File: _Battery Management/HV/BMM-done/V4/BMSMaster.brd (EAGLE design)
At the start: 83.8 x 91.4 mm, 113 parts, among them J1 M2S02B-PASK-2(LF)(SN), J10 IMD, J14 USB_B_RA, J2 M2S02B-PASK-2(LF)(SN), J3 M8S08B-PASK-2(LF)(SN), J5 M16_M_194280016, J6 M2770166, J7 M2770166, J8 M2770166, J9 M2770166, K1 ADJ14024, Q1 IRFR9120TRPBF, Q3 BSS123, U1 SN75HVD08DRMSOP, U10 NC7S14M5X, U11 LTC6820, U12 FT24C64A, U23 NUD3160DMT1G, U3 FT230X, U4 SN74LVC2G241, U5 NC7S14M5X, U6 DSPIC33FJ128GP804, U7 DMG6602SVTQ, U8 LTC6820, U9 MAX823TEUK+T_3.08, Y1 12Mhz

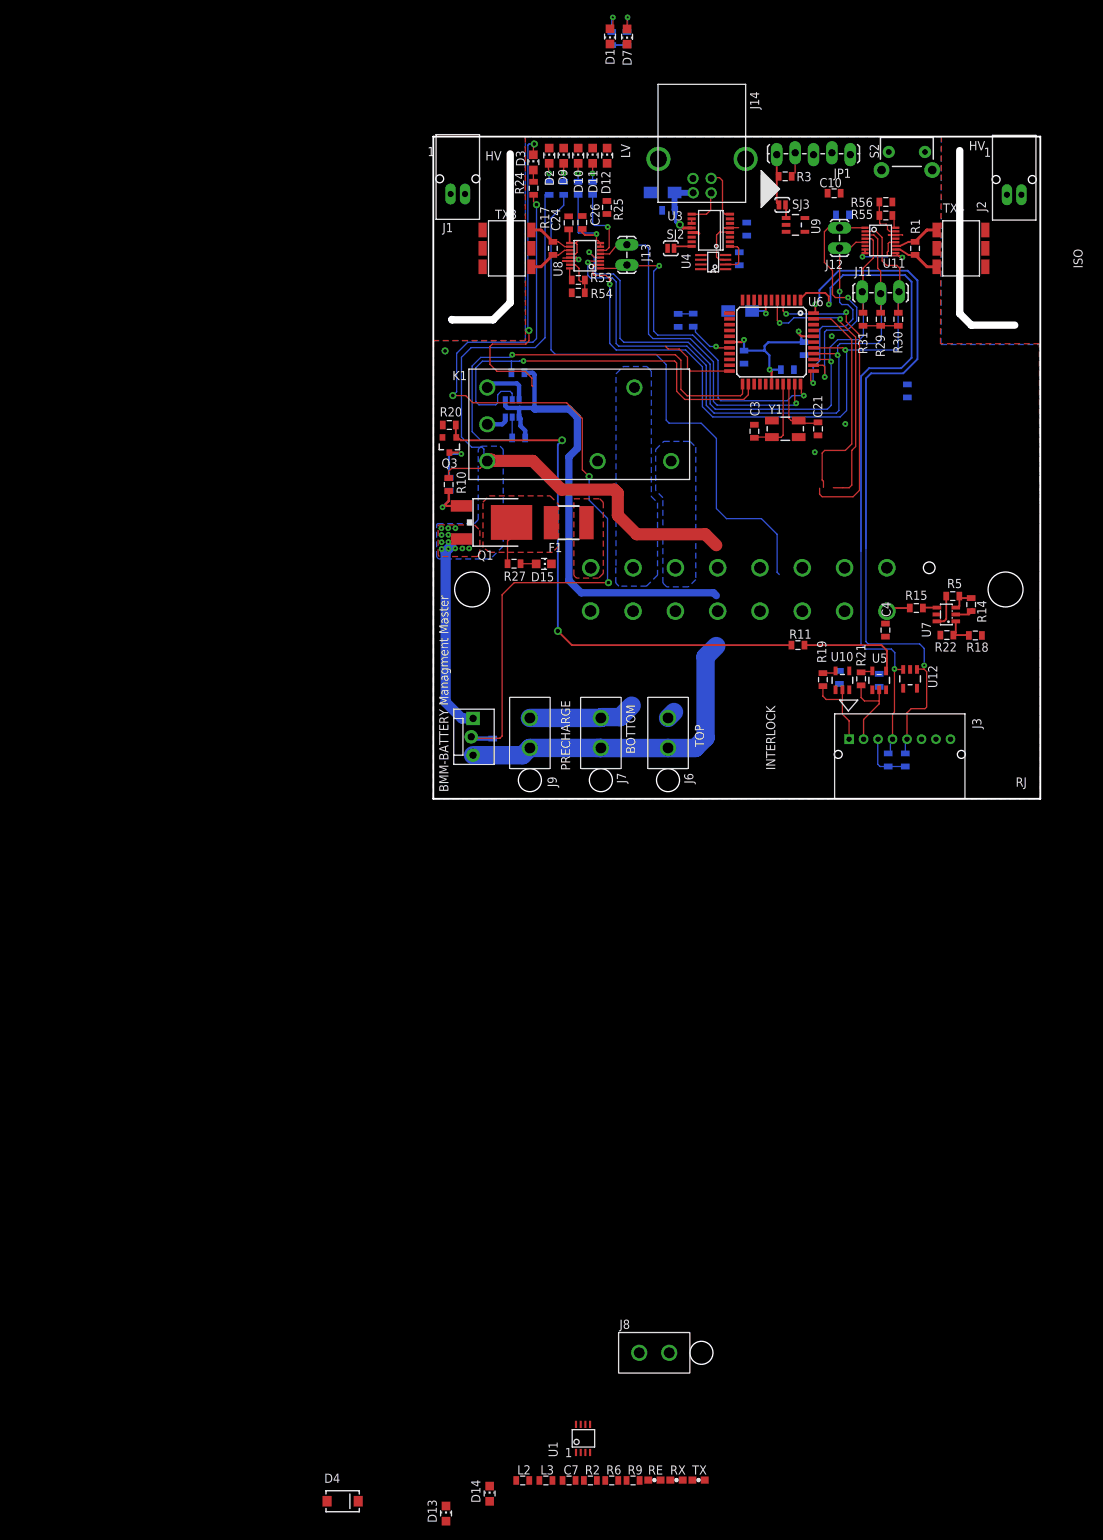
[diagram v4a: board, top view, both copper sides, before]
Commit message: Working on DC/DC power supply
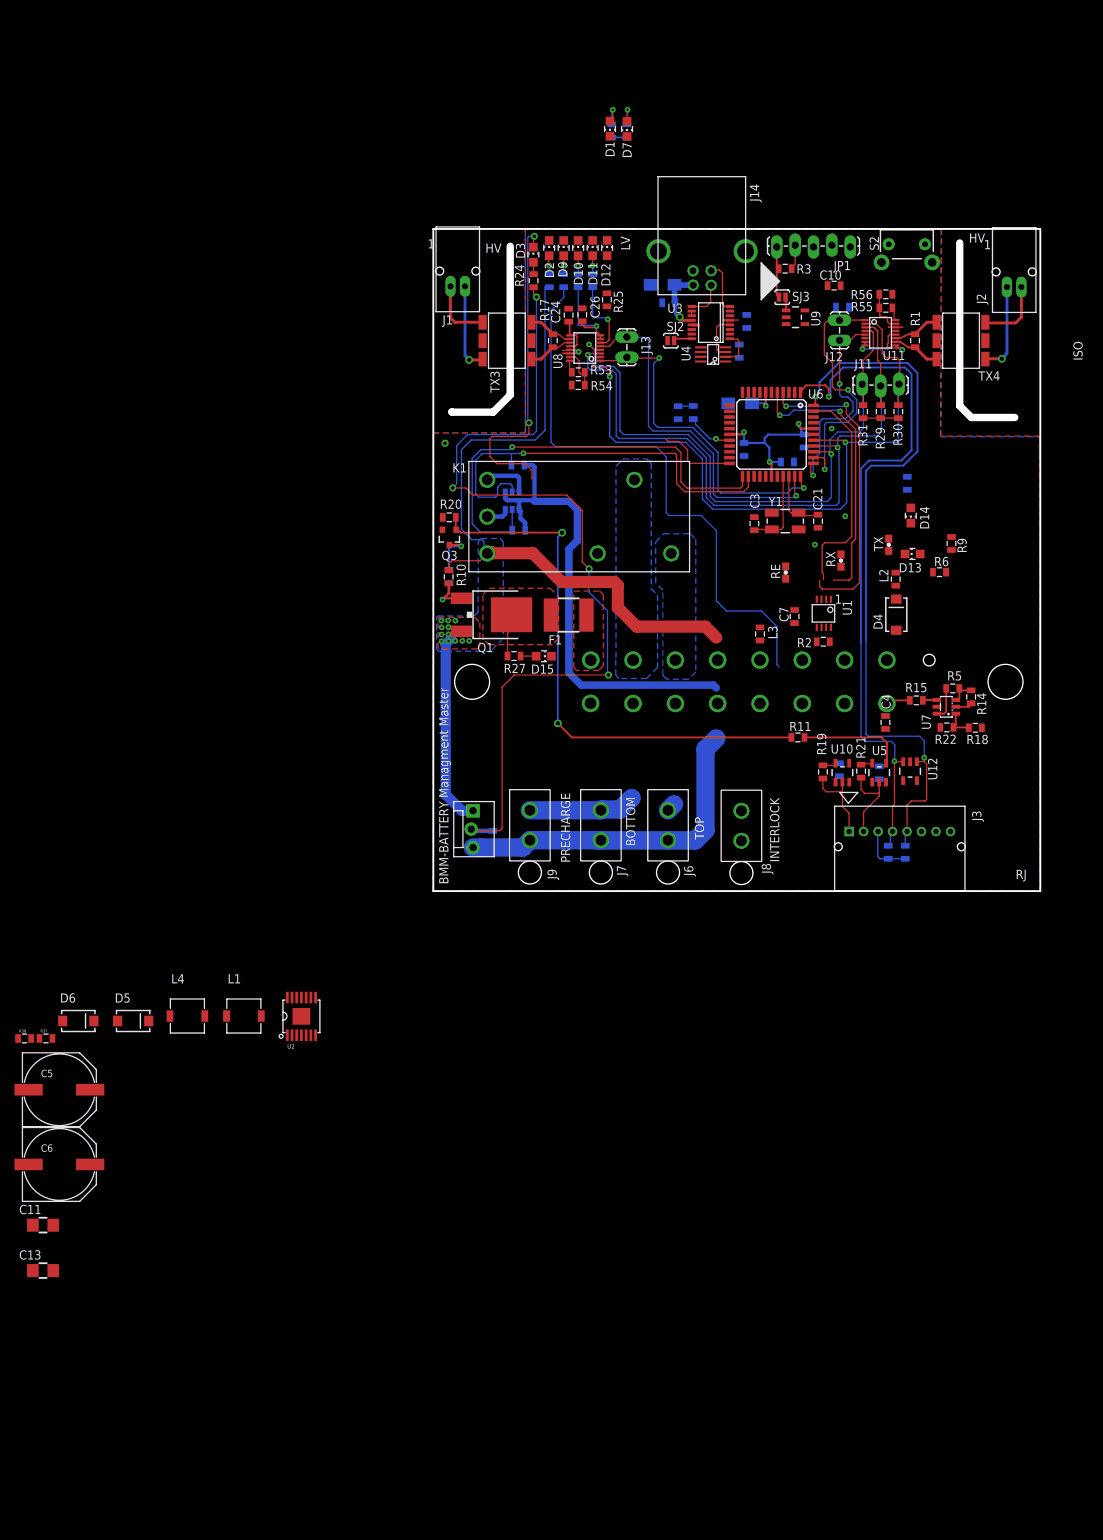
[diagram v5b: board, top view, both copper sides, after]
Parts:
- added C11, C13: 10UF, FSAE Electric:1206
- added C5, C6: 100UF, FSAE Electric:PANASONIC-G
- added D5, D6: DIODE_S1B, FSAE Electric:SMA
- added L1, L4: (no value), FSAE Electric:VLF5014AT
- added R37, R38: 20K, FSAE Electric:0805
- added U2: TPS54386PWPR, FSAE Electric:TSSOP-14
- moved D13 147.3 mm to (66.2, 46.5), turned to 90 degrees
- moved D14 147.1 mm to (65.9, 51.8), turned to 180 degrees
- moved D4 144.3 mm to (63.9, 38.1), turned to 90 degrees
- moved R9 136.7 mm to (71.6, 48.0), turned to 270 degrees
- moved L2 134.7 mm to (63.9, 43.0), turned to 270 degrees
- moved R6 133.3 mm to (69.9, 44.0)
- moved TX 131.8 mm to (62.9, 47.8), turned to 90 degrees
- moved RX 129.0 mm to (56.3, 45.6), turned to 90 degrees
- moved RE 126.6 mm to (48.7, 43.9), turned to 90 degrees
- moved C7 123.3 mm to (49.9, 37.9), turned to 90 degrees
- moved L3 120.6 mm to (45.1, 35.5), turned to 270 degrees
- moved R2 120.2 mm to (53.8, 34.4), turned to 180 degrees
- moved U1 118.7 mm to (53.9, 38.3), turned to 180 degrees
- moved J8 73.8 mm to (42.5, 8.97), turned to 270 degrees
- moved J2 12.8 mm to (80.2, 83.4)
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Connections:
- removed net N$60: L3.1
- new net N$56: L1.2, U2.3
- new net N$57: L4.1, U2.12
- new net N$59: R37.1, U2.7
- new net N$61: R38.1, U2.8
- net +3V3: now also C13.1, C6.+, L4.2, R38.2
- net +5V: now also C11.1, C5.+, L1.1, R37.2
- net +9V: now also U2.1, U2.14
- net GND: now also C11.2, C13.2, C5.-, C6.-, L3.1, U2.4, U2.5, U2.6, U2.EP
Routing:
- net N$55: track 0.00 -> 12.5 mm, vias 0 -> 1
- net N$33: track 0.00 -> 12.3 mm, vias 0 -> 1
- net N$53: track 0.00 -> 9.51 mm
- net N$34: track 0.00 -> 9.05 mm

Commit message: 
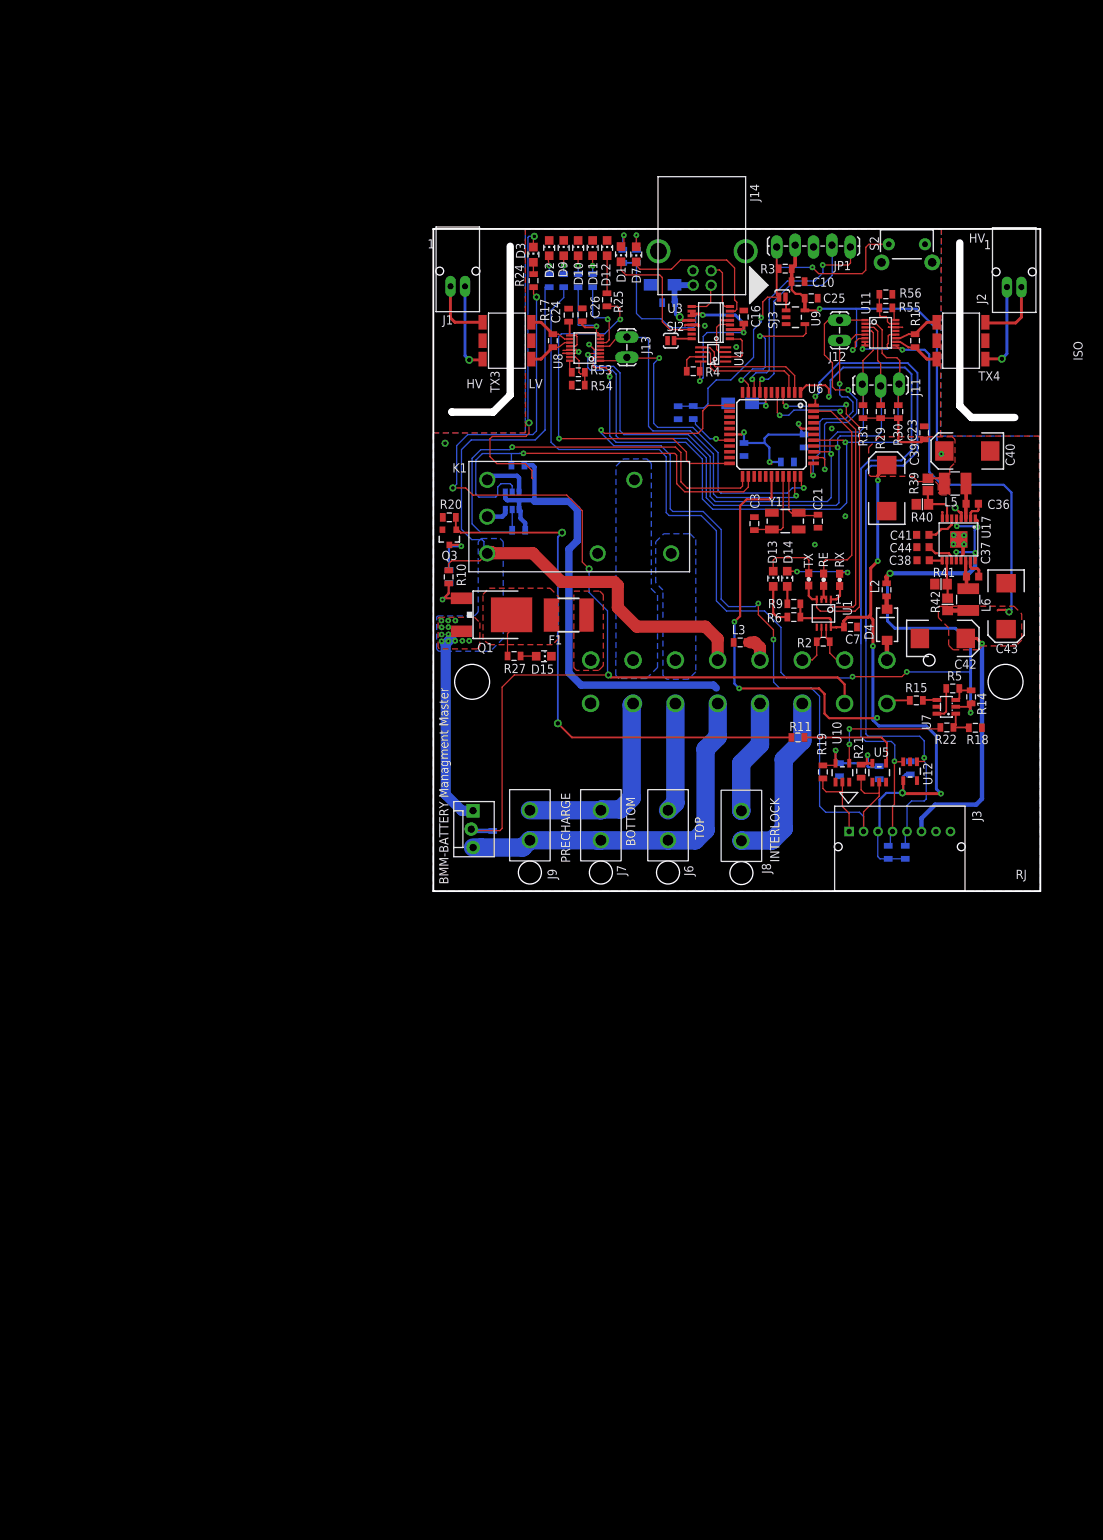
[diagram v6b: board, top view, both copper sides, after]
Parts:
- removed C11, C13: 10UF, FSAE Electric:1206
- removed C5, C6: 100UF, FSAE Electric:PANASONIC-G
- removed D5, D6: DIODE_S1B, FSAE Electric:SMA
- removed L1, L4: (no value), FSAE Electric:VLF5014AT
- removed R37, R38: 20K, FSAE Electric:0805
- removed U2: TPS54386PWPR, FSAE Electric:TSSOP-14
- added C36, C37: 0.1UF, DFT2:R0603
- added C38: 1UF, DFT2:R0603
- added C39, C40, C42, C43: 22UF, DFT2:EIA7343
- added C41, C44: 0.001UF, DFT2:R0603
- added L5: L_2.2UH, DFT2:LQH43
- added L6: L_4.7UH, DFT2:LQH43
- added R39: 73.2K, DFT2:R0805
- added R40, R41: 22.1K, DFT2:R0805
- added R42: 124K, DFT2:R0805
- added U17: TPS542951PWPR, DFT2:TSSOP-16
- moved R9 23.3 mm to (49.8, 39.6), turned to 0 degrees
- moved R6 21.0 mm to (49.8, 37.8)
- moved D13 19.6 mm to (46.9, 43.1), turned to 0 degrees
- moved D14 19.2 mm to (48.9, 43.1), turned to 0 degrees
- moved D1 17.4 mm to (25.9, 87.9)
- moved R7 17.4 mm to (26.2, 87.6)
- moved R8 17.4 mm to (28.1, 87.6)
- moved D7 17.4 mm to (28.0, 87.9)
- moved TX 12.0 mm to (51.8, 43.0)
- moved C7 7.86 mm to (57.6, 36.4), turned to 0 degrees
- moved C23 7.34 mm to (67.8, 63.2), flipped to the top, turned to 90 degrees
- moved C4 7.15 mm to (65.9, 17.0), flipped to the bottom, turned to 90 degrees
- moved R4 6.94 mm to (35.9, 71.7), flipped to the top, turned to 0 degrees
- moved RE 5.33 mm to (53.9, 43.0)
- moved C10 5.01 mm to (50.4, 84.1)
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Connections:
- removed net N$56: L1.2, U2.3
- removed net N$57: L4.1, U2.12
- removed net N$59: R37.1, U2.7
- removed net N$61: R38.1, U2.8
- new net N$100: C38.1, U17.9
- new net N$101: R39.1, R40.2, U17.7
- new net N$102: C41.1, U17.6
- new net N$103: R41.2, R42.1, U17.10
- new net N$77: C44.1, U17.11
- new net N$94: C36.1, U17.2
- new net N$97: C36.2, L5.2, U17.3
- new net N$98: C37.1, U17.15
- new net N$99: C37.2, L6.1, U17.14
- net +3V3: now also C39.+, C40.+, L5.1, R39.2; no longer C13.1, C6.+, L4.2, R38.2
- net +5V: now also C42.+, C43.+, L6.2, R42.2; no longer C11.1, C5.+, L1.1, R37.2
- net +9V: now also U17.1, U17.12, U17.16, U17.5; no longer U2.1, U2.14
- net GND: now also C38.2, C39.-, C40.-, C41.2, C42.-, C43.-, C44.2, R40.1, R41.1, U17.13, U17.4, U17.8, U17.EP; no longer C11.2, C13.2, C5.-, C6.-, U2.4, U2.5, U2.6, U2.EP
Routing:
- net +3V3: track 49.4 -> 252.3 mm, vias 4 -> 15
- net HV-SENSE: track 12.1 -> 118.3 mm, vias 0 -> 3
- net +5V: track 37.5 -> 142.4 mm, vias 3 -> 7
- net +9V: track 83.0 -> 171.4 mm, vias 0 -> 8
- net 3V: track 2.73 -> 49.2 mm, vias 0 -> 3
- net N$45: track 9.55 -> 54.8 mm, vias 0 -> 2
- net N$44: track 11.2 -> 52.7 mm, vias 0 -> 2
- net IMD: track 123.7 -> 159.5 mm
- net N$48: track 0.00 -> 31.0 mm, vias 0 -> 2
- net N$47: track 0.00 -> 27.6 mm, vias 0 -> 1
- net INTERLOCK_IN: track 0.00 -> 24.9 mm
- net N$8: track 0.00 -> 22.2 mm
- net RX2: track 38.8 -> 58.2 mm, vias 2 -> 4
- net WDI: track 0.00 -> 19.1 mm, vias 0 -> 2
- net USB_RX: track 0.00 -> 18.0 mm
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- added copper zone on layer 1, net +3V3
- added copper zone on layer 1, net +5V

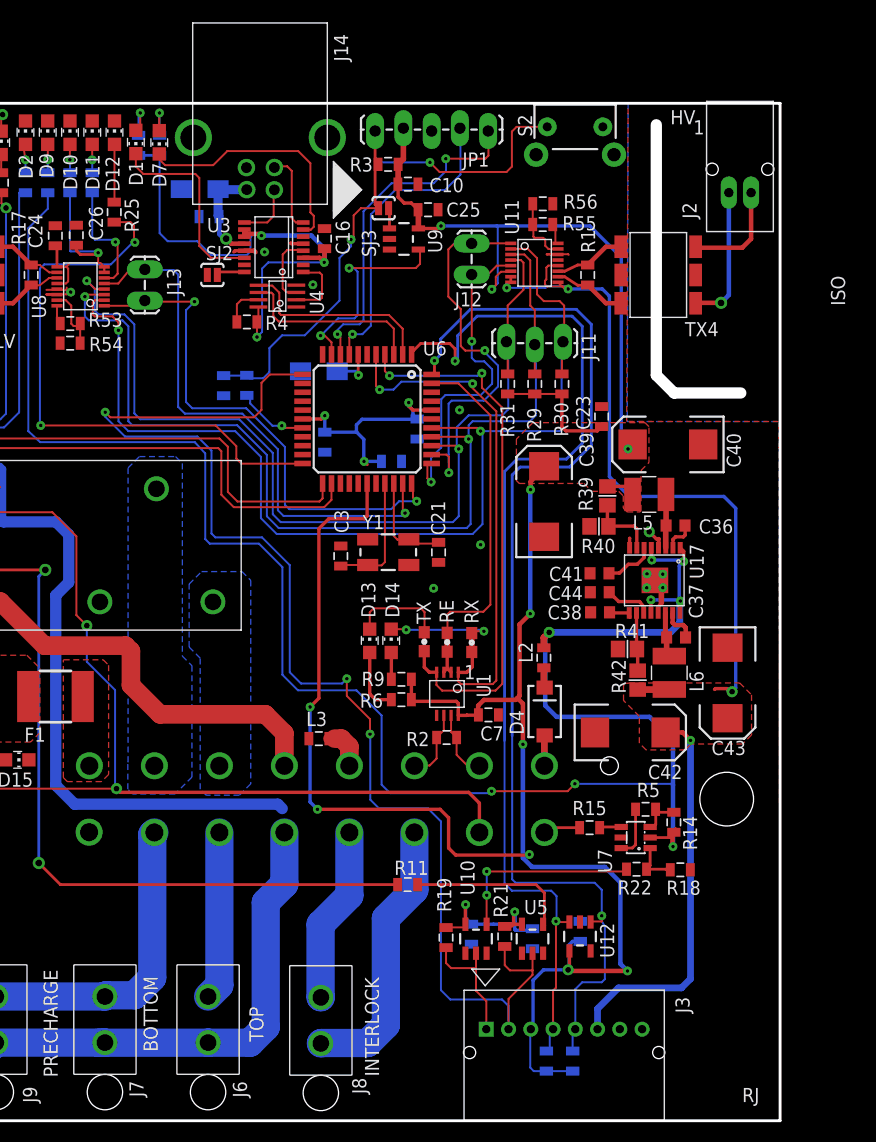
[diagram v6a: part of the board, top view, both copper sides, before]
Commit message: 
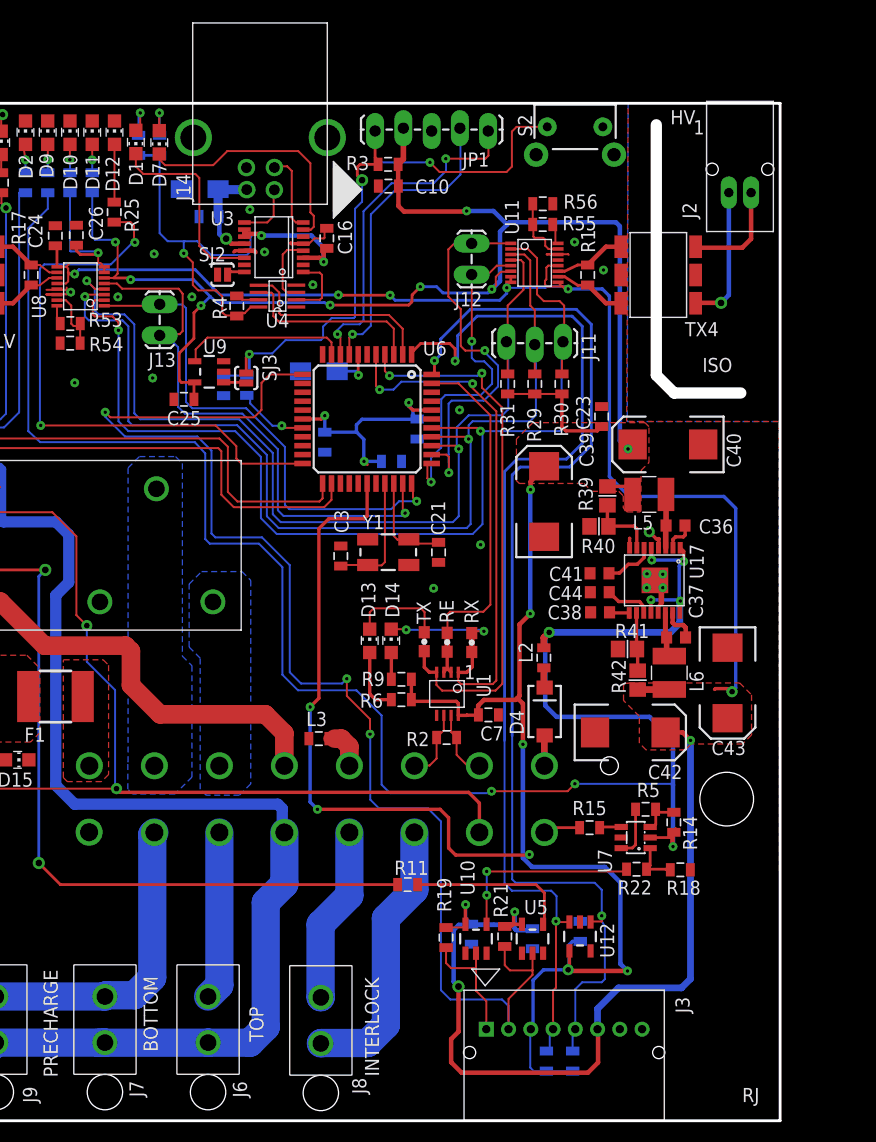
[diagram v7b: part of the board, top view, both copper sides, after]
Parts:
- moved C25 27.8 mm to (30.2, 64.8), turned to 180 degrees
- moved U9 21.2 mm to (32.5, 67.3), turned to 90 degrees
- moved SJ3 19.6 mm to (35.8, 66.7), turned to 90 degrees
- moved J13 5.82 mm to (28.1, 70.7), turned to 90 degrees
- moved C10 1.76 mm to (48.6, 83.9), turned to 180 degrees
- moved R4 1.69 mm to (35.0, 73.2), turned to 270 degrees
- moved SJ2 0.91 mm to (33.7, 76.0)
- moved C16 0.20 mm to (43.1, 79.3)
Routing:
- net +5V: track 142.4 -> 220.6 mm, vias 7 -> 11
- net +3V3: track 252.3 -> 302.2 mm, vias 15 -> 19
- net WDI: track 19.1 -> 15.0 mm, vias 2 -> 0
- net N$45: track 54.8 -> 58.3 mm, vias 2 -> 3
- net GND: track 18.2 -> 21.4 mm, vias 12 -> 20
- net VSS: track 165.7 -> 167.9 mm
- net EN2: track 47.2 -> 45.5 mm, vias 2 -> 1
- net N$69: track 3.70 -> 2.06 mm
- net 3V: track 49.2 -> 47.8 mm
- net CS2: track 49.9 -> 51.1 mm
- net N$43: track 2.62 -> 1.67 mm
